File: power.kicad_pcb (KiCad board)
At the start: 2 copper layers, 66.2 x 41 mm, 23 parts, among them J1 USB_C_Receptacle, J2 AVR-ISP-6, J3 Screw_Terminal_01x02, U1 INA226, U2 AMS1117-3.3, U3 ATmega328P-A, Y1 Crystal

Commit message: Fixed the few small changes from my revert
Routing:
- net VBUS: track 63.2 -> 80.8 mm, vias 2 -> 4
- net Net-(J1-CC2): track 6.60 -> 9.27 mm
- net +5V: track 168.3 -> 169.8 mm
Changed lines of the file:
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@@
+	)
+	(segment
+		(start 170.241176 84)
+		(end 171 84)
+		(width 0.2)
+		(layer "F.Cu")
+		(net 7)
 	)
 	(segment
@@
 	)
 	(segment
+		(start 165.75 79.7)
+		(end 163.35 77.3)
+		(width 0.2)
+		(layer "F.Cu")
+		(net 7)
+	)
+	(segment
+		(start 112.109202 68)
+		(end 111.5 68.609202)
+		(width 0.2)
+		(layer "F.Cu")
+		(net 7)
+	)
+	(segment
+		(start 113.341143 71.374447)
+		(end 112.874447 71.374447)
+		(width 0.2)
+		(layer "F.Cu")
+		(net 7)
+	)
+	(segment
+		(start 167.675 81.433824)
+		(end 170.241176 84)
+		(width 0.2)
+		(layer "F.Cu")
+		(net 7)
+	)
+	(segment
+		(start 113.5 68)
+		(end 112.5 68)
+		(width 0.2)
+		(layer "F.Cu")
+		(net 7)
+	)
+	(segment
 		(start 160.5 77.5)
 		(end 162.749 77.5)
@@
 	)
 	(segment
+		(start 111.5 68.609202)
+		(end 111.5 69.5)
+		(width 0.2)
+		(layer "F.Cu")
+		(net 7)
+	)
+	(segment
+		(start 112.5 68)
+		(end 112.109202 68)
+		(width 0.2)
+		(layer "F.Cu")
+		(net 7)
+	)
+	(segment
+		(start 112.874447 71.374447)
+		(end 112.5 71)
+		(width 0.2)
+		(layer "F.Cu")
+		(net 7)
+	)
+	(segment
+		(start 113.75 68.25)
+		(end 113.5 68)
+		(width 0.2)
+		(layer "F.Cu")
+		(net 7)
+	)
+	(segment
+		(start 167.675 80.5)
+		(end 167.675 81.433824)
+		(width 0.2)
+		(layer "F.Cu")
+		(net 7)
+	)
+	(segment
 		(start 114 67.5)
 		(end 114 68)
@@
 		(net 7)
 	)
+	(segment
+		(start 165.75 80.5)
+		(end 165.75 79.7)
+		(width 0.2)
+		(layer "F.Cu")
+		(net 7)
+	)
 	(via
 		(at 165.75 80.5)
+		(size 0.6)
+		(drill 0.3)
+		(layers "F.Cu" "B.Cu")
+		(free yes)
+		(net 7)
+	)
+	(via
+		(at 111.5 69.5)
+		(size 0.6)
+		(drill 0.3)
+		(layers "F.Cu" "B.Cu")
+		(net 7)
+	)
+	(via
+		(at 113.341143 71.374447)
 		(size 0.6)
 		(drill 0.3)
@@
 	)
 	(segment
+		(start 113.21559 71.5)
+		(end 113.341143 71.374447)
+		(width 0.2)
+		(layer "B.Cu")
+		(net 7)
+	)
+	(segment
+		(start 111.5 69.5)
+		(end 111.5 71)
+		(width 0.2)
+		(layer "B.Cu")
+		(net 7)
+	)
+	(segment
+		(start 111.5 71)
+		(end 112 71.5)
+		(width 0.2)
+		(layer "B.Cu")
+		(net 7)
+	)
+	(segment
 		(start 115.5 69)
 		(end 116 69)
@@
 	)
 	(segment
+		(start 112 71.5)
+		(end 113.21559 71.5)
+		(width 0.2)
+		(layer "B.Cu")
+		(net 7)
+	)
+	(segment
 		(start 160.586193 69.711133)
 		(end 160.789923 69.711133)
@@
 	)
 	(segment
-		(start 114.337365 71.426)
-		(end 112.035202 71.426)
+		(start 116.296665 69.4667)
+		(end 113.763365 72)
 		(width 0.2)
 		(layer "F.Cu")
@@
 	)
 	(segment
-		(start 112.035202 71.426)
-		(end 111.824 71.214798)
+		(start 110.776 71.099698)
+		(end 110.776 70.5)
 		(width 0.2)
 		(layer "F.Cu")
@@
 	)
 	(segment
-		(start 111.824 71.214798)
-		(end 111.824 70.785202)
+		(start 113.763365 72)
+		(end 111.676302 72)
 		(width 0.2)
 		(layer "F.Cu")
@@
 	)
 	(segment
-		(start 111.824 70.785202)
-		(end 112.109202 70.5)
+		(start 111.676302 72)
+		(end 110.776 71.099698)
 		(width 0.2)
 		(layer "F.Cu")
@@
 	)
 	(segment
-		(start 114.337365 71.426)
-		(end 116.296665 69.4667)
-		(width 0.2)
-		(layer "F.Cu")
-		(net 28)
-	)
-	(segment
-		(start 112.109202 70.5)
+		(start 110.776 70.5)
 		(end 112.5 70.5)
 		(width 0.2)
@@
 		(width 0.2)
 		(layer "F.Cu")
+		(net 42)
+	)
+	(segment
+		(start 171 83.5)
+		(end 171 82)
+		(width 0.2)
+		(layer "F.Cu")

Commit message: Final fixes
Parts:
- moved C1 2.15 mm to (161.9, 77.5)
- moved C2 2.15 mm to (174.2, 74.3)
- moved C3 2.15 mm to (158.2, 65.0)
- moved C4 2.15 mm to (165.9, 70.5)
- moved J2 2.15 mm to (161.4, 53.4)
- moved R1 2.15 mm to (165.7, 85.0)
- moved R2 2.15 mm to (165.6, 86.6)
- moved R6 2.15 mm to (169.7, 57.5)
- moved R7 2.15 mm to (170.7, 80.5)
- moved U2 2.15 mm to (168.7, 75.0)
- moved U3 2.15 mm to (169.2, 63.5)
- moved R5 2.15 mm to (172.8, 57.5)
- moved R9 2.15 mm to (166.3, 57.5)
- moved U1 2.15 mm to (170.9, 84.5)
- moved Y1 1.13 mm to (159.5, 69.5)
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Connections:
- J1 pad A9: +5V -> VBUS
- U1 pad 1: unconnected-(U1-A1-Pad1) -> GND
- U1 pad 2: unconnected-(U1-A0-Pad2) -> GND
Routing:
- net +5V: track 169.8 -> 165.2 mm
- net SCL: track 82.4 -> 86.4 mm
- net SDA: track 74.6 -> 78.6 mm
- net VBUS: track 80.8 -> 84.1 mm
- net 3V3: track 123.6 -> 125.2 mm
- net Net-(U3-XTAL1/PB6): track 9.04 -> 10.5 mm
- net GND: track 55.7 -> 57.0 mm
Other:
- board size 66.2 x 41 mm -> 68.2 x 41 mm

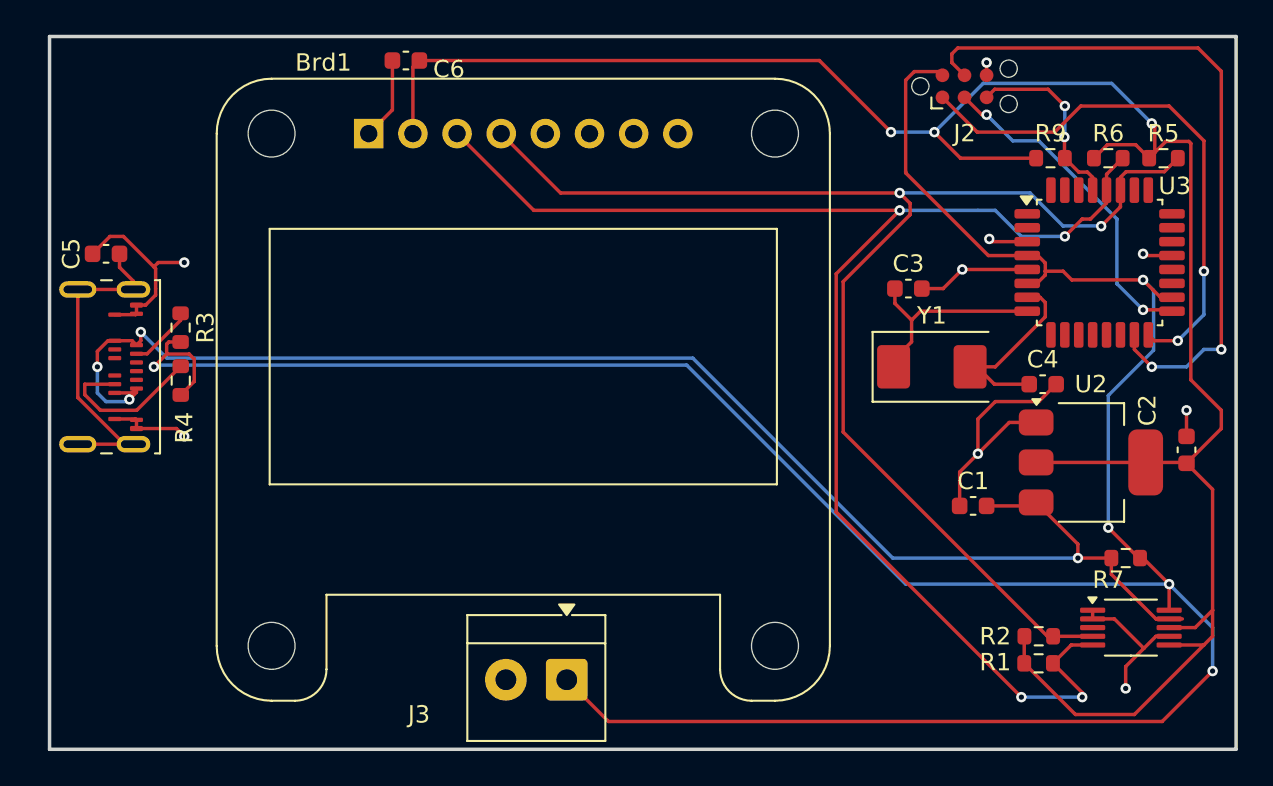
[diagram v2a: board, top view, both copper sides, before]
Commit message: Switched USB C out to the proper one
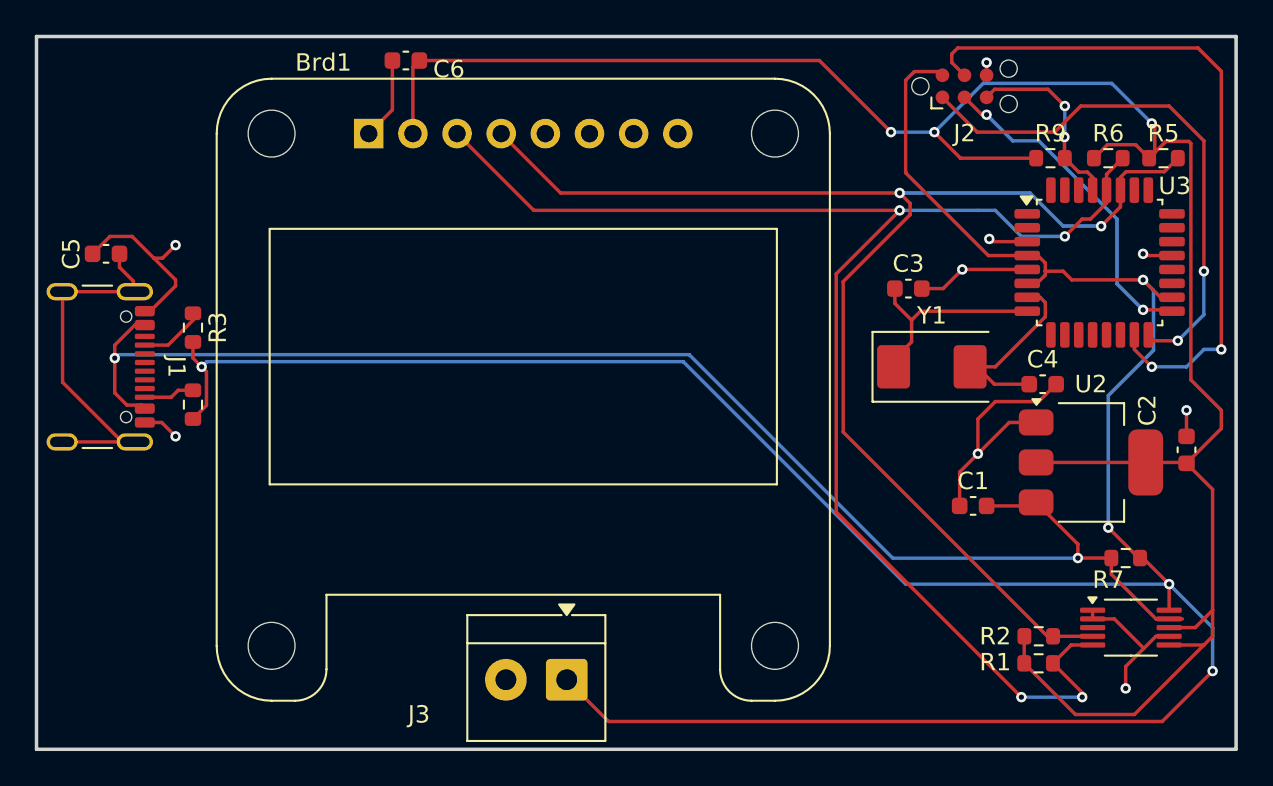
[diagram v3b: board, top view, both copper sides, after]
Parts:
- J1: footprint Connector_USB:USB_C_Receptacle_Amphenol_124019772112A -> Connector_USB:USB_C_Receptacle_GCT_USB4105-xx-A_16P_TopMnt_Horizontal
- moved R4 1.55 mm to (117.0, 71.7)
- moved R3 0.71 mm to (117.0, 67.2)
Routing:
- net Net-(J1-CC2): track 9.27 -> 2.94 mm
- net +5V: track 165.2 -> 161.2 mm
- net GND: track 57.0 -> 53.2 mm
- net Net-(J1-SHIELD): track 19.3 -> 22.2 mm
- net VBUS: track 84.1 -> 82.1 mm, vias 4 -> 2
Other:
- board size 68.2 x 41 mm -> 69 x 41 mm
